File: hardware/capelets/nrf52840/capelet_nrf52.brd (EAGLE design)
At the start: 54.6 x 38.1 mm, 2 parts

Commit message: hardware: updated capelets
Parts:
- added LED1: 598-8130-107FLED_0805, shepherd:LEDC2012X75
- added R1: 100R, shepherd:RESC2012X65
- added R2: 10k, shepherd:RESC2012X65
- added R3: 50R, shepherd:RESC2012X65
- added T1: SI2374DSSOT23-VSHAY, shepherd:SOT95P237X112-3
- U$1: value SHPRD_CPLT_T -> SHPRD_CPLT_NRF52; device mylib:SHPRD_CPLT_T -> shepherd:SHPRD_CPLT_NRF52
- U$2: device mylib:NRF52840-DONGLE -> shepherd:NRF52840-DONGLE
- moved U$2 91.6 mm to (-0.38, -42.4)
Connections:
- new net GPIO_LED: R2.1, R3.1, U$2.P0.02
- new net N$1: R3.2, T1.1
- new net N$3: LED1.1, T1.3
- new net N$4: LED1.2, R1.1
- net GND: now also R2.2, T1.2
- net V_SUP: now also R1.2
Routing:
- net V_SUP: track 26.4 -> 61.7 mm
- net SWDCLK: track 36.4 -> 31.0 mm
- net GPIO_LED: track 0.00 -> 4.78 mm
- net SWDIO: track 35.3 -> 30.5 mm
- net UART_TX: track 11.9 -> 7.97 mm
- net UART_RX: track 11.9 -> 7.97 mm
- net N$1: track 0.00 -> 3.79 mm
- net N$3: track 0.00 -> 3.29 mm
- net N$4: track 0.00 -> 2.66 mm
- net GPIO3: track 7.33 -> 8.53 mm
- net GPIO1: track 7.33 -> 8.53 mm
- net GPIO0: track 7.33 -> 8.53 mm
- net GPIO2: track 7.33 -> 8.53 mm, vias 1 -> 0
- net V_BATOK: track 9.76 -> 9.12 mm
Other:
- board size 54.6 x 38.1 mm -> 54.6 x 41.9 mm
- board text added: "SHEPHERD v1.4 CAPELET NRF52"
- board text removed: "SHEPHERD v1.3 CAPELET NRF52"

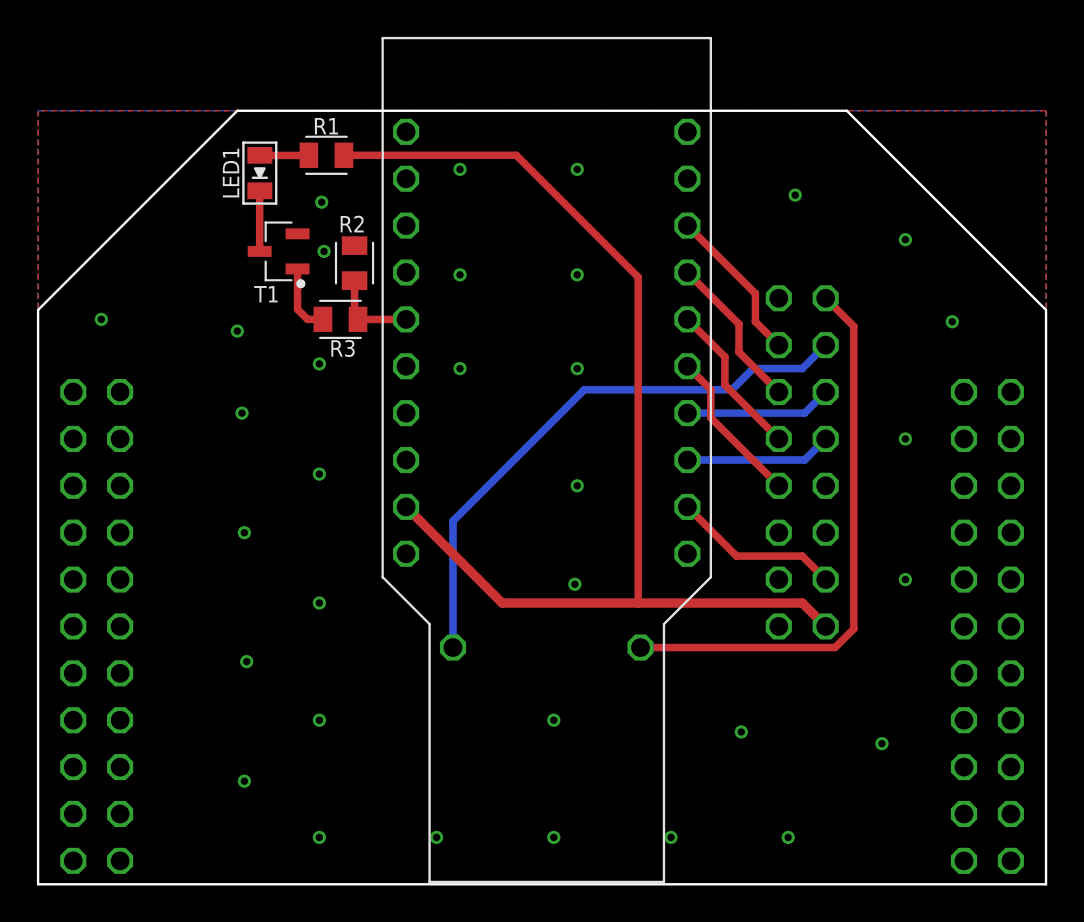
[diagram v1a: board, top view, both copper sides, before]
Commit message: hardware: prepared capelets for external manufacturing
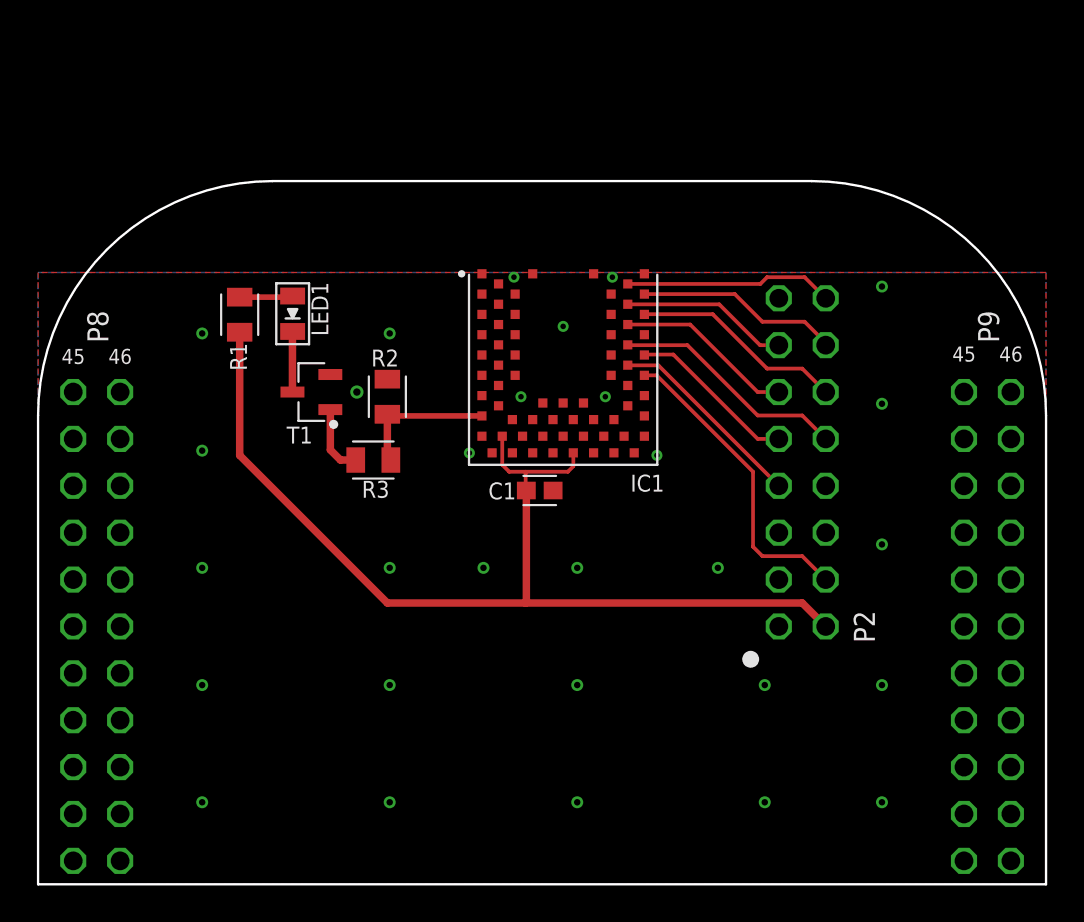
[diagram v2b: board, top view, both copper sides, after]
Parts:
- removed U$1: SHPRD_CPLT_NRF52, shepherd:SHPRD_CPLT_NRF52
- removed U$2: NRF52840-DONGLE, shepherd:NRF52840-DONGLE
- added C1: 4.7u, shepherd:CAPC1608X95
- added IC1: BMD-340-A-R, shepherd:RIGADO_BMD-340-A-R
- added P2: (no value), pinhead:2X08
- added P8, P9: (no value), pinhead:2X11
- added U$3: (no value), shepherd:SHPRD_CPLT_T
- R1: value 100R -> 130R
- R3: value 50R -> 130R
- moved R1 9.83 mm to (-17.0, -38.4), turned to 270 degrees
- moved R3 7.82 mm to (-9.78, -46.2)
- moved T1 7.82 mm to (-13.1, -42.5)
- moved LED1 7.82 mm to (-14.1, -38.3)
- moved R2 7.45 mm to (-9.02, -42.8)
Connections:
- removed net VDD_3V3: U$1.P2$5
- new net VBUS: IC1.66
- net GND: now also C1.2, IC1.1, IC1.16, IC1.18, IC1.2, IC1.29, IC1.3, IC1.30, IC1.4, IC1.45, IC1.46, IC1.47, IC1.5, IC1.55, P2.1, P2.15, P2.8; no longer U$1.P2$16, U$1.P2$2, U$1.P2$7, U$1.P9$43, U$1.P9$44, U$1.P9$45, U$1.P9$46, U$2.GND@1, U$2.GND@2, U$2.GND@3
- net GPIO0: now also IC1.37, P2.9; no longer U$1.P2$10, U$2.P0.24
- net GPIO1: now also IC1.42, P2.13; no longer U$1.P2$14, U$2.P0.09
- net GPIO2: now also IC1.36, P2.7; no longer U$1.P2$8, U$2.P0.22
- net GPIO3: now also IC1.40, P2.11; no longer U$1.P2$12, U$2.P1.00
- net GPIO_LED: now also IC1.15; no longer U$2.P0.02
- net SWDCLK: now also IC1.43, P2.14; no longer U$1.P2$13, U$2.SWDCLK
- net SWDIO: now also IC1.44, P2.16; no longer U$1.P2$15, U$2.SWDIO
- net UART_RX: now also IC1.41, P2.12; no longer U$1.P2$11, U$2.P0.20
- net UART_TX: now also IC1.38, P2.10; no longer U$1.P2$9, U$2.P0.17
- net V_BATOK: now also IC1.35, P2.4; no longer U$1.P2$3, U$2.P0.15
- net V_SUP: now also C1.1, IC1.17, IC1.65, P2.2; no longer U$1.P2$1, U$2.VDDOUT
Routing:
- net SWDCLK: track 31.0 -> 11.0 mm
- net SWDIO: track 30.5 -> 11.3 mm
- net V_BATOK: track 9.12 -> 16.8 mm
- net V_SUP: track 61.7 -> 55.8 mm
- net UART_TX: track 7.97 -> 12.8 mm
- net UART_RX: track 7.97 -> 11.6 mm
- net GPIO_LED: track 4.78 -> 7.72 mm
- net GPIO2: track 8.53 -> 10.9 mm
- net GPIO3: track 8.53 -> 9.70 mm
- net GPIO0: track 8.53 -> 9.19 mm
- net GPIO1: track 8.53 -> 9.10 mm
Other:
- board size 54.6 x 41.9 mm -> 54.6 x 38.1 mm
- board text added: "45"
- board text added: "46"
- board text added: "P2: Pins pointing to bottom, solder on top"
- board text added: "P8: Pins pointing to bottom, solder on top"
- board text added: "P9: Pins pointing to bottom, solder on top"
- board text added: "SHEPHERD v1.5 CAPELET NRF52"
- board text removed: "SHEPHERD v1.4 CAPELET NRF52"
